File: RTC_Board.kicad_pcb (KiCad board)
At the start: 2 copper layers, 30 x 24 mm, 8 parts, among them J1 Conn_01x01, J2 Conn_01x01, J3 Conn_01x01, J4 Conn_01x01, U1 DS3231MZ

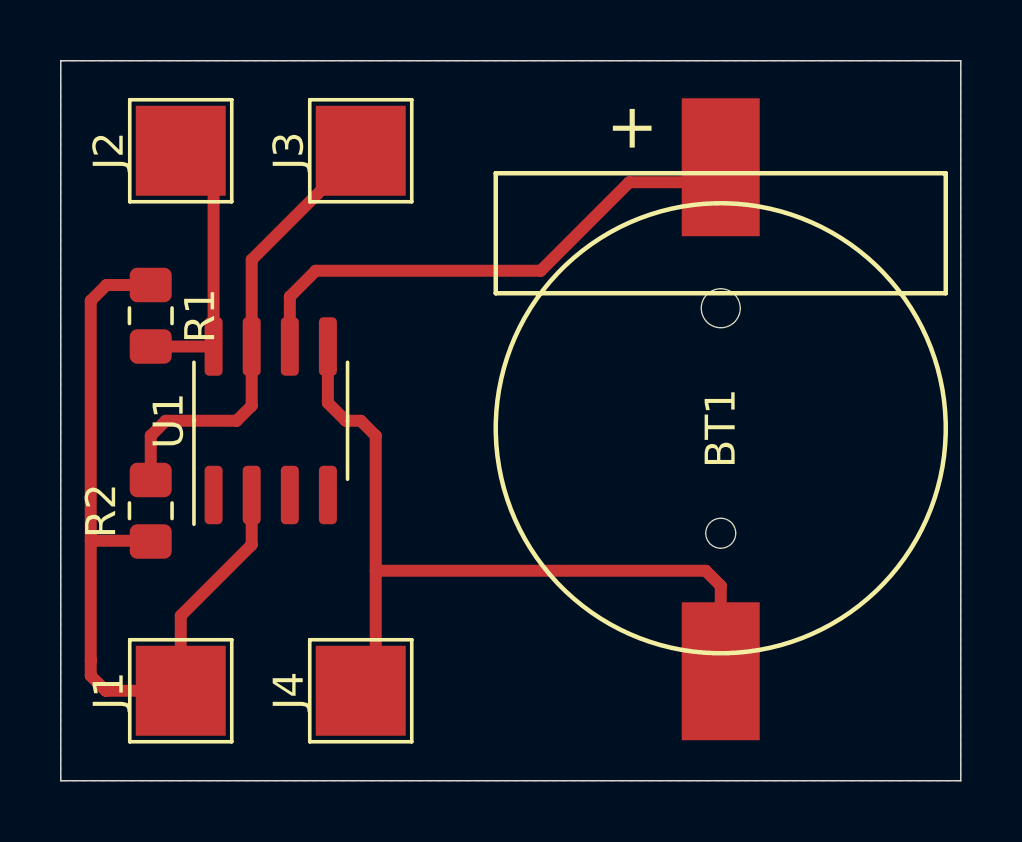
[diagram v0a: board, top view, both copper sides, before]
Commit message: decoupling cap
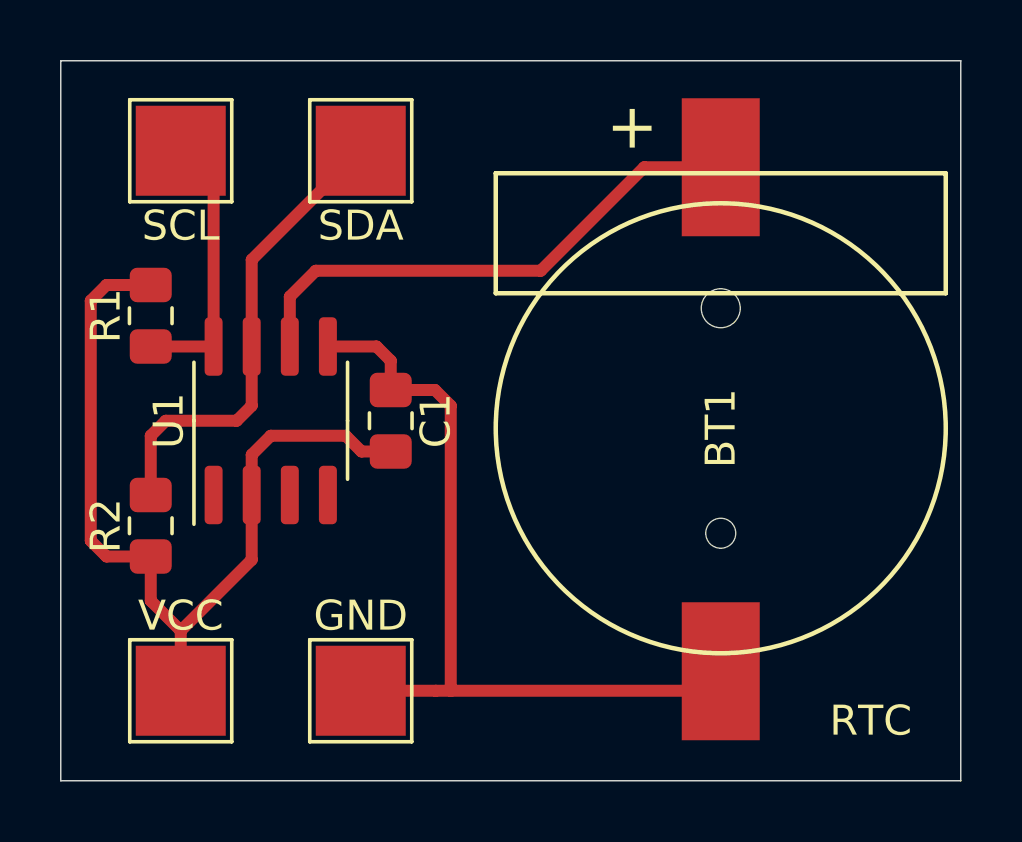
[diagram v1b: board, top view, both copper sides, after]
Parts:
- added C1: 100n, Capacitor_SMD:C_0805_2012Metric_Pad1.15x1.40mm_HandSolder, F.Cu at (131.0, 100.0)
- moved R2 0.50 mm to (123.0, 103.5)
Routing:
- net VCC: track 27.0 -> 29.3 mm
- net GND: track 26.7 -> 27.3 mm
- removed copper zone on F.Cu, net (none)
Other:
- board text added: "GND"
- board text added: "RTC"
- board text added: "SCL"
- board text added: "SDA"
- board text added: "VCC"
